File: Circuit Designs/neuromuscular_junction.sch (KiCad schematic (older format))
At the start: 8 parts

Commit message: added the MCU, duplicated the LEDs for bottom side, changed the can driver to tcan330
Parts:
- removed U?: TJA1051TK-3, Package_DFN_QFN:DFN-8-1EP_3x3mm_P0.65mm_EP1.55x2.4mm, symbol Interface_CAN_LIN:TJA1051TK-3
- added R? (x2): 10K, Resistor_SMD:R_0402_1005Metric, symbol CoE_Resistor:10K
- added R? (x2): 22R, Resistor_SMD:R_0402_1005Metric, symbol CoE_Resistor:22R
- added U?: TCAN330, Package_TO_SOT_SMD:TSOT-23-8, symbol CoE_IntegratedCircuit:TCAN330
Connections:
- net labels added: +3V3
- net labels removed: +3.3V, +5V
- wire segments 21 -> 33
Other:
- moved on the sheet: C?

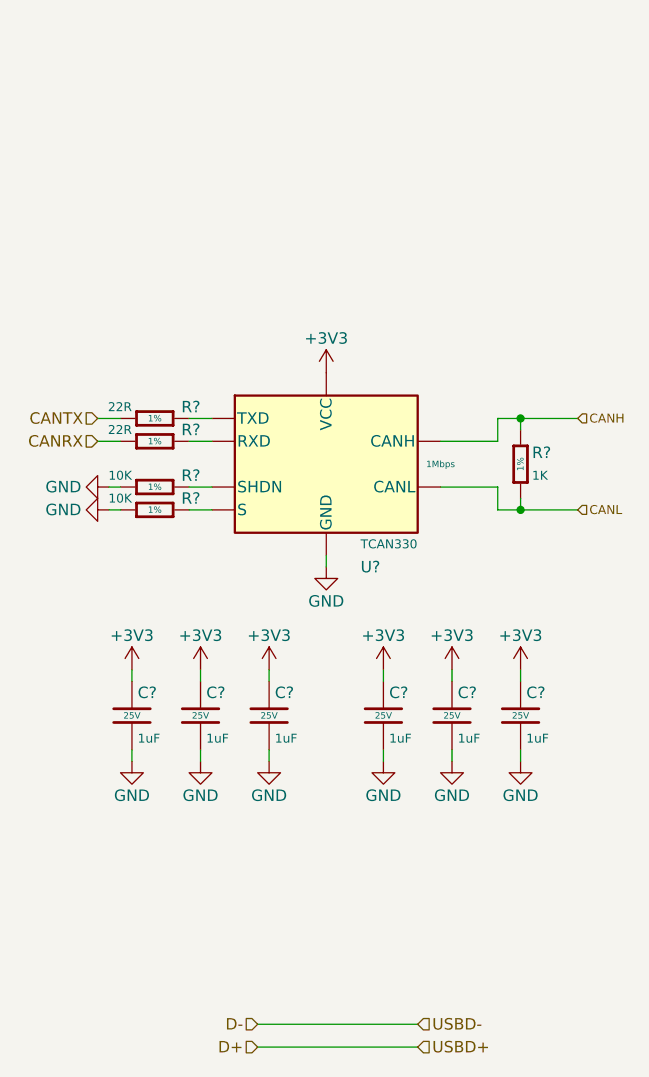
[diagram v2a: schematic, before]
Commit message: added servo control input feature
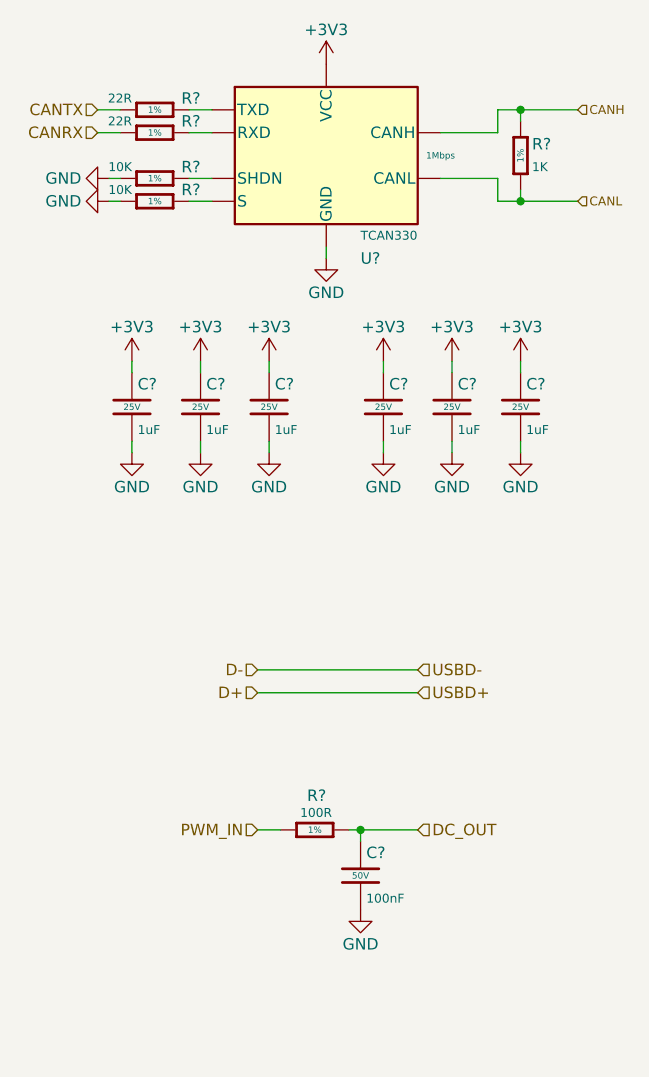
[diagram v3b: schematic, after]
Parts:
- added C?: 100nF, Capacitor_SMD:C_0402_1005Metric, symbol CoE_Capacitor:100nF
- added R?: 100R, Resistor_SMD:R_0402_1005Metric, symbol CoE_Resistor:100R
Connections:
- net GND: now also C?.2
- new net DC_OUT: C?.1, R?.2
- new net PWM_IN: R?.1
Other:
- moved on the sheet: C?, R?, U?

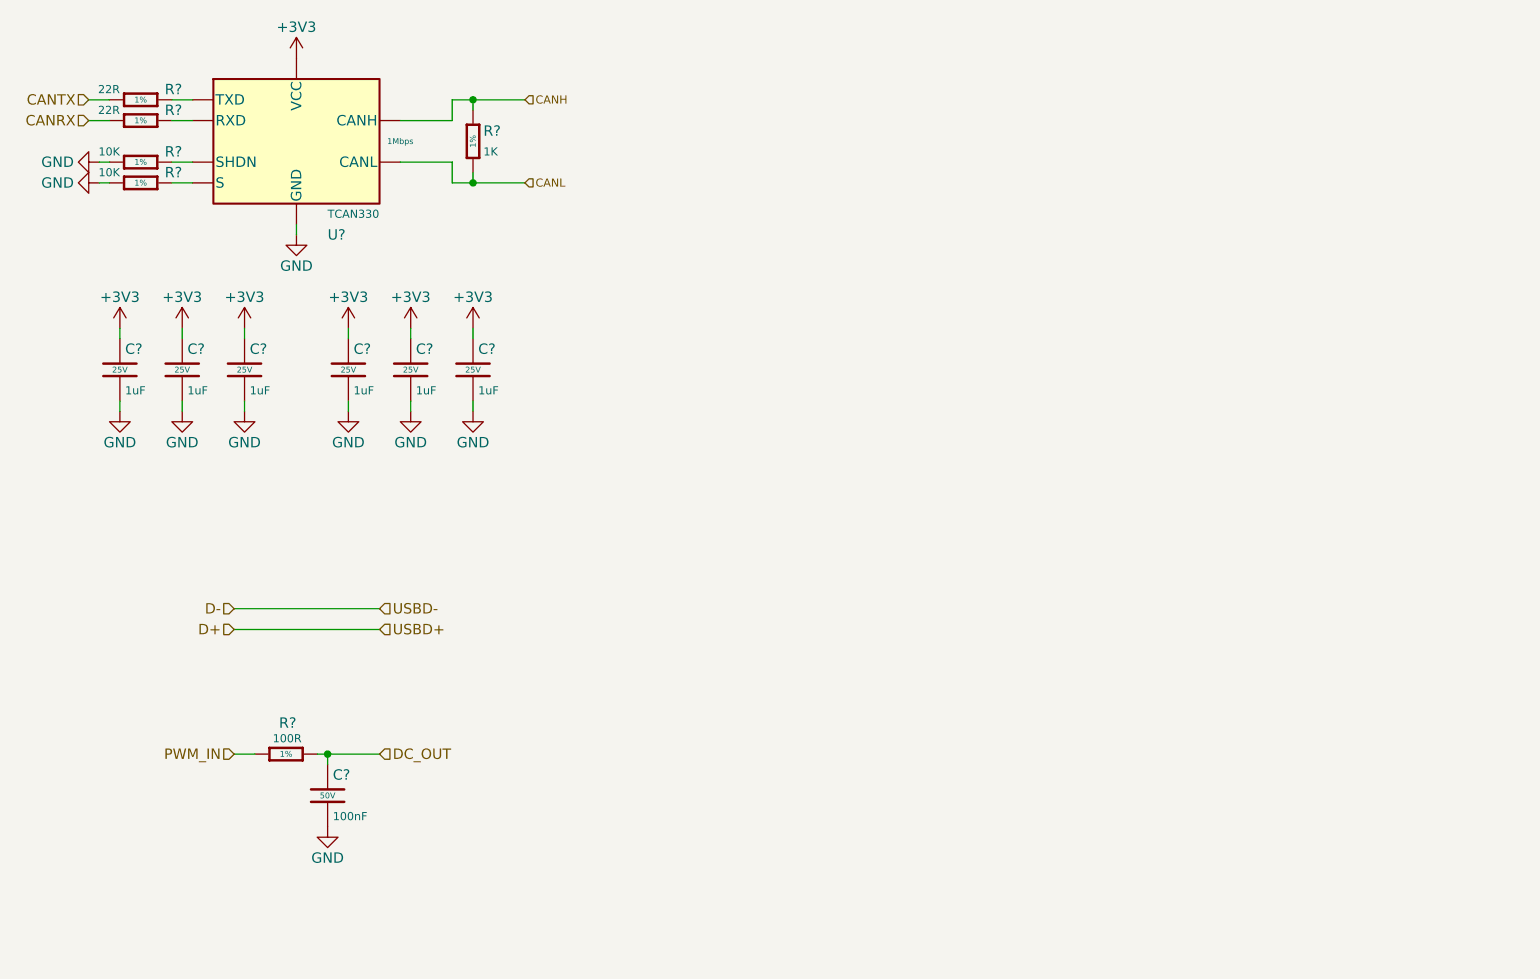
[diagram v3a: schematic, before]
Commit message: edited myofibril file, added a related image about myofibrils
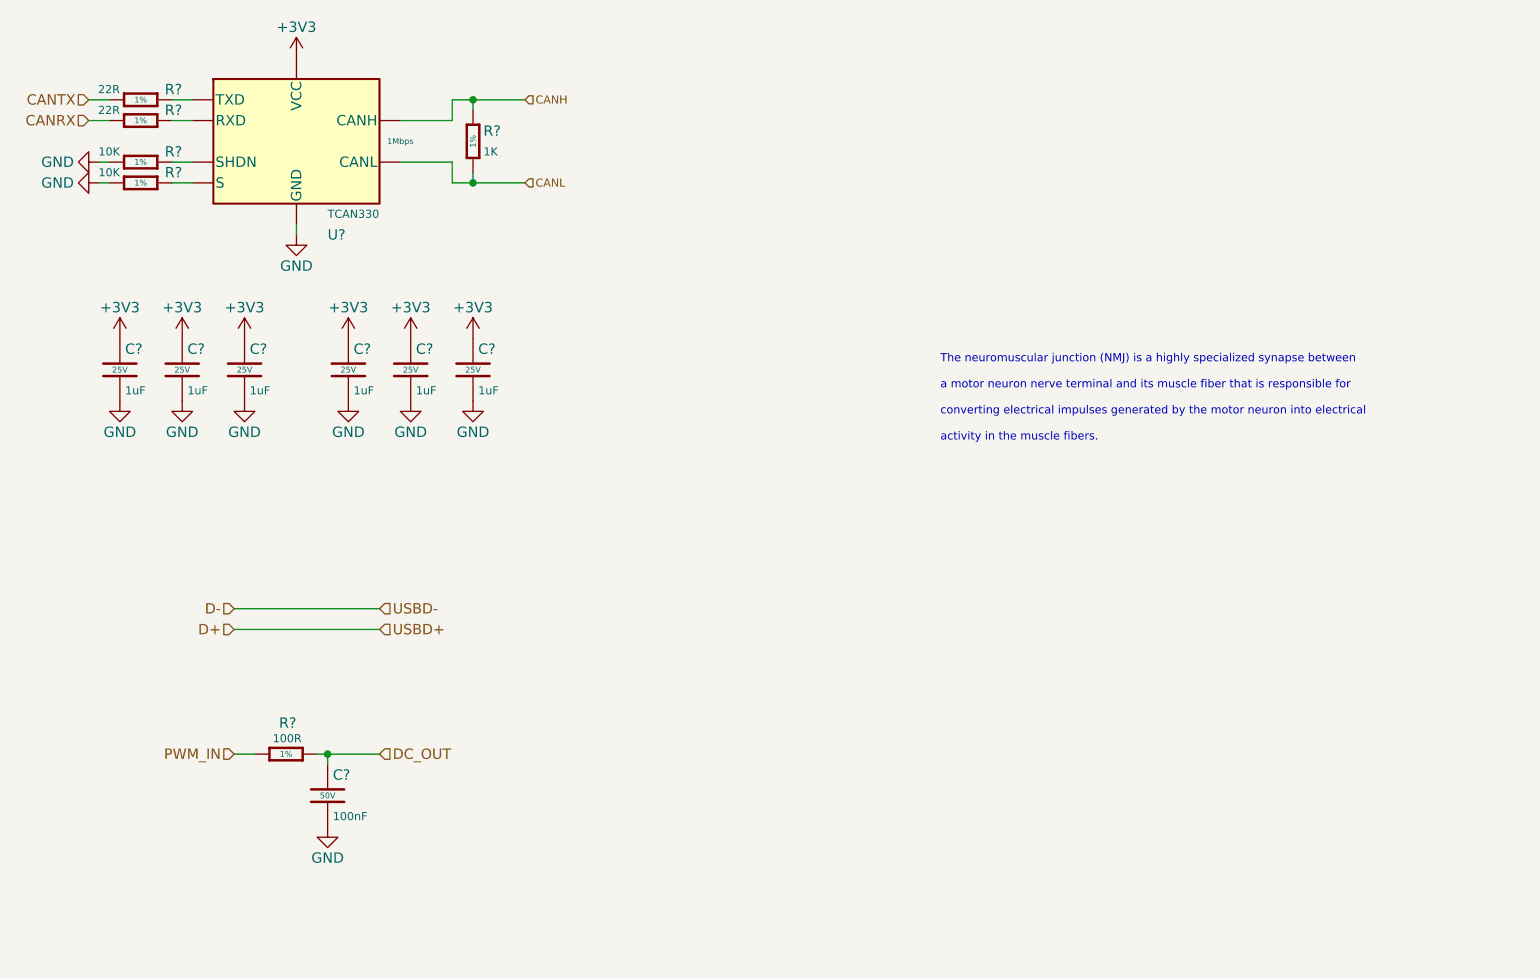
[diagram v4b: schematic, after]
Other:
- note added: "The neuromuscular junction (NMJ) is a highly specialized synapse between \n\na motor neuron nerve terminal and its muscle fiber that is responsible for \n\nconverting electrical impulses generated by the motor neuron into electrical \n\nactivity in the muscle fibers."
